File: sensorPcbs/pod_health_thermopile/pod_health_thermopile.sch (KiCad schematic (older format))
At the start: 2 parts, among them J1 RJ45, U1 TMP007

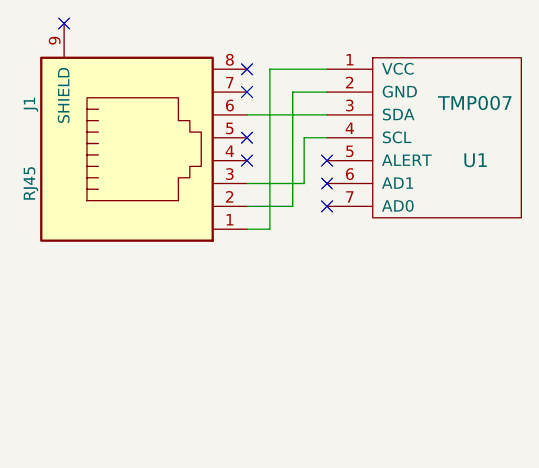
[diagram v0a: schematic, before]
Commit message: changed all the sensor PCB schematics and added the global component schematic library into each project
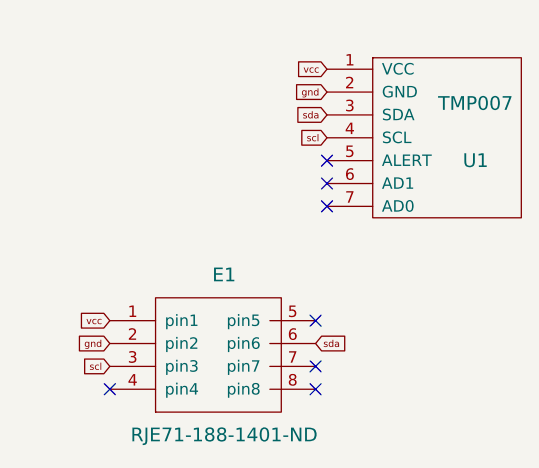
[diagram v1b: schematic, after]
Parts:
- removed J1: RJ45, Connectors:RJ45_8, symbol RJ45
- added E1: RJE71-188-1401-ND, symbol RJE71-188-1401-ND
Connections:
- net vcc: now reaches U1.1 (VCC)
- net vcc: now also E1.1 (pin1)
- net gnd: now reaches U1.2 (GND)
- net gnd: now also E1.2 (pin2)
- net scl: now reaches U1.4 (SCL)
- net scl: now also E1.3 (pin3)
- net sda: now reaches U1.3 (SDA)
- net sda: now also E1.6 (pin6)
- no-connect marks 8 -> 7
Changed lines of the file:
@@
 EESchema Schematic File Version 2
-LIBS:power
-LIBS:device
-LIBS:transistors
-LIBS:conn
-LIBS:linear
-LIBS:regul
-LIBS:74xx
-LIBS:cmos4000
-LIBS:adc-dac
-LIBS:memory
-LIBS:xilinx
-LIBS:microcontrollers
-LIBS:dsp
-LIBS:microchip
-LIBS:analog_switches
-LIBS:motorola
-LIBS:texas
-LIBS:intel
-LIBS:audio
-LIBS:interface
-LIBS:digital-audio
-LIBS:philips
-LIBS:display
-LIBS:cypress
-LIBS:siliconi
-LIBS:opto
-LIBS:atmel
-LIBS:contrib
-LIBS:valves
 LIBS:tmp007
+LIBS:customSchematics
 LIBS:pod_health_thermopile-cache
 EELAYER 25 0
@@
 $EndDescr
 $Comp
-L RJ45 J1
-U 1 1 58DAB1D1
-P 3450 2650
-F 0 "J1" H 3650 3150 50  0000 C CNN
-F 1 "RJ45" H 3300 3150 50  0000 C CNN
-F 2 "Connectors:RJ45_8" H 3450 2650 50  0001 C CNN
-F 3 "" H 3450 2650 50  0001 C CNN
-	1    3450 2650
-	0    -1   -1   0
-$EndComp
-$Comp
 L TMP007 U1
 U 1 1 58DAB48D
@@
 NoConn ~ 4250 2800
 NoConn ~ 4250 2700
-NoConn ~ 3100 2100
-Wire Wire Line
-	4250 2300 4000 2300
-Wire Wire Line
-	4000 2300 4000 3000
-Wire Wire Line
-	4000 3000 3900 3000
-Wire Wire Line
-	4250 2400 4100 2400
-Wire Wire Line
-	4100 2400 4100 2900
-Wire Wire Line
-	4100 2900 3900 2900
-Wire Wire Line
-	4250 2600 4150 2600
-Wire Wire Line
-	4150 2600 4150 2800
-Wire Wire Line
-	4150 2800 3900 2800
-Wire Wire Line
-	4250 2500 3900 2500
-NoConn ~ 3900 2300
-NoConn ~ 3900 2400
-NoConn ~ 3900 2600
-NoConn ~ 3900 2700
+$Comp
+L RJE71-188-1401-ND E1
+U 1 1 5971202C
+P 3500 3400
+F 0 "E1" H 3800 3600 60  0000 C CNN
+F 1 "RJE71-188-1401-ND" H 3800 2900 60  0000 C CNN
+F 2 "" H 3500 3400 60  0001 C CNN
+F 3 "" H 3500 3400 60  0001 C CNN
+	1    3500 3400
+	1    0    0    -1
+$EndComp
+Text GLabel 3300 3400 0    30   Input ~ 0
+vcc
+Text GLabel 3300 3500 0    30   Input ~ 0
+gnd
+Text GLabel 3300 3600 0    30   Input ~ 0
+scl
+Text GLabel 4200 3500 2    30   Input ~ 0
+sda
+Text GLabel 4250 2300 0    30   Input ~ 0
+vcc
+Text GLabel 4250 2400 0    30   Input ~ 0
+gnd
+Text GLabel 4250 2500 0    30   Input ~ 0
+sda
+Text GLabel 4250 2600 0    30   Input ~ 0
+scl
+NoConn ~ 4200 3400
+NoConn ~ 4200 3600
+NoConn ~ 4200 3700
+NoConn ~ 3300 3700
 $EndSCHEMATC

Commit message: added all the ferkin new ethernet shields to the sensor pcbs
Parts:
- E1: footprint (none) -> footprints:RJE71-188-1401-ND
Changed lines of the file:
@@
 F 0 "E1" H 3800 3600 60  0000 C CNN
 F 1 "RJE71-188-1401-ND" H 3800 2900 60  0000 C CNN
-F 2 "" H 3500 3400 60  0001 C CNN
+F 2 "footprints:RJE71-188-1401-ND" H 3500 3400 60  0001 C CNN
 F 3 "" H 3500 3400 60  0001 C CNN
 	1    3500 3400
